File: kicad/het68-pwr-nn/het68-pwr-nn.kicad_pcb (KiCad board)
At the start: 2 copper layers, 140 x 80 mm, 64 parts, among them J1 CT_SEC, J2 USB_C, J3 VOUT, Q1 X0202MN, Q2 AO3400A, Q3 AO3401A, Q4 AO3400A

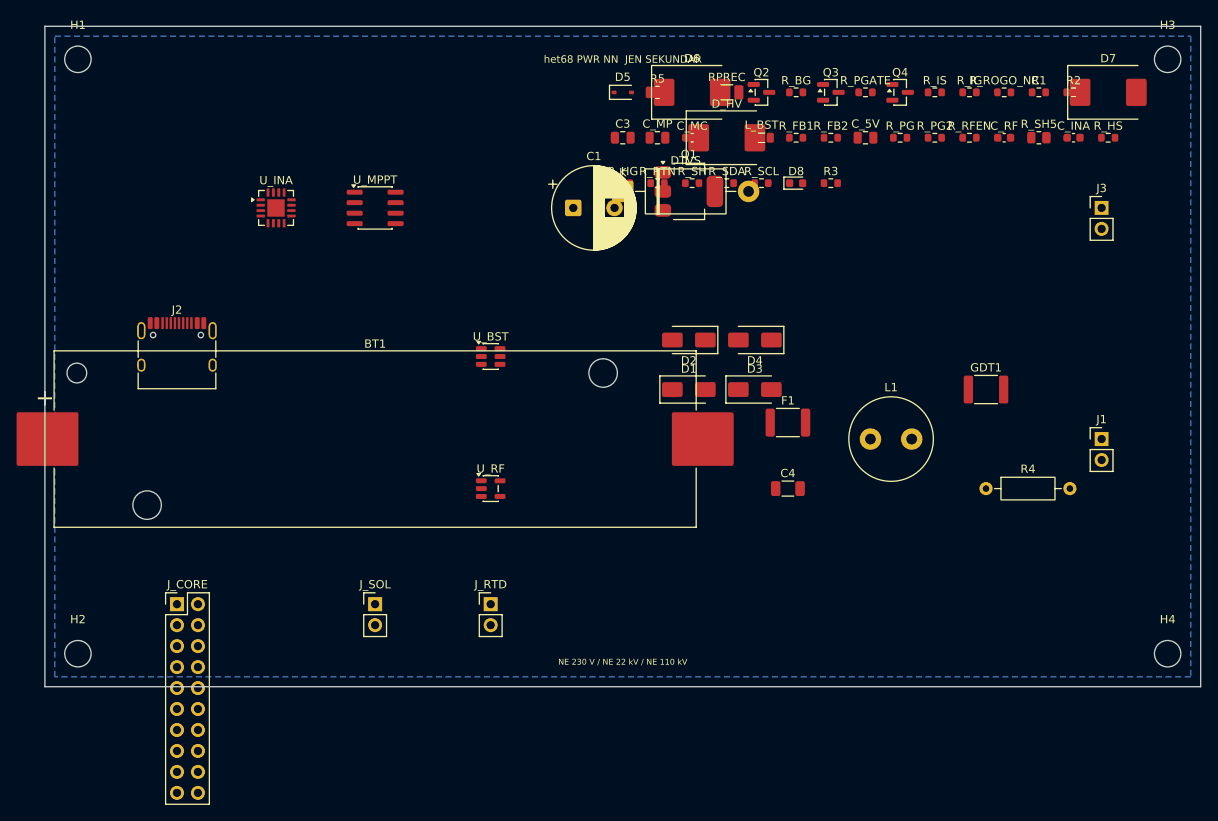
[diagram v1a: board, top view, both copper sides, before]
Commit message: Add a Core status LED and three buttons, and fit a 21700 holder.
RESET, BOOT and USER sit on the east edge with one SK6812; the power board uses a Keystone 1122 instead of an 18650 sled. Masks, schematics and JLCPCB gerber zips are in the tree.

Co-authored-by: Cursor <cursoragent@cursor.com>
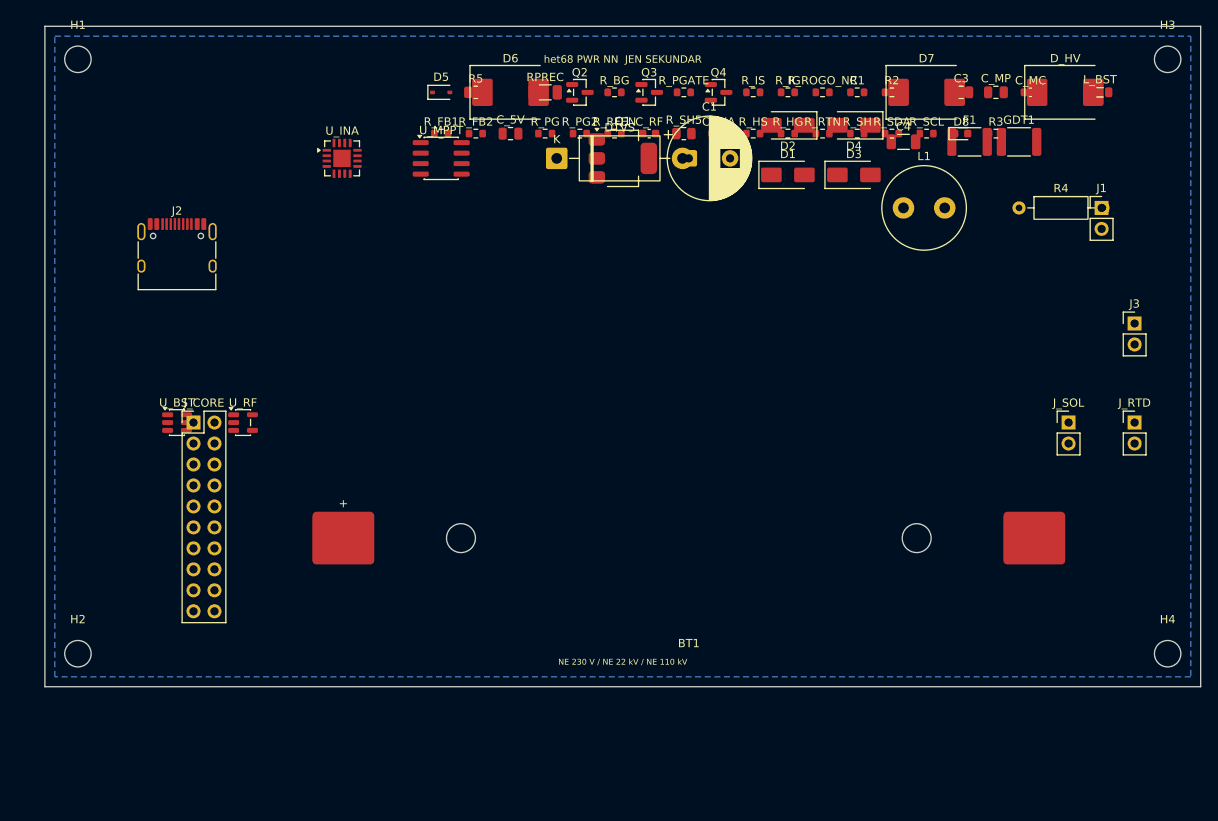
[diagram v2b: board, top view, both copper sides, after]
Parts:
- BT1: value LiFePO4_1S -> 21700; footprint Battery:BatteryHolder_Keystone_1042_1x18650 -> het68:Keystone_1122_21700
- moved J_SOL 86.8 mm to (124.0, 48.0)
- moved J_RTD 81.0 mm to (132.0, 48.0)
- moved C4 44.3 mm to (104.0, 14.0)
- moved R_HS 43.0 mm to (85.8, 13.0)
- moved C_5V 43.0 mm to (56.4, 13.0)
- moved C_INA 43.0 mm to (81.6, 13.0)
- moved C_RF 43.0 mm to (73.2, 13.0)
- moved R_FB1 43.0 mm to (48.0, 13.0)
- moved R_FB2 43.0 mm to (52.2, 13.0)
- moved R_PG2 43.0 mm to (64.8, 13.0)
- moved R_RFEN 43.0 mm to (69.0, 13.0)
- moved R_SH5 43.0 mm to (77.4, 13.0)
- moved R_PG 43.0 mm to (60.6, 13.0)
- moved C3 41.4 mm to (111.0, 8.00)
- moved C_MC 41.4 mm to (119.4, 8.00)
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
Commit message: Route signal copper on the five v4 boards and drop tracks that still short.
Core and the satellite have no copper shorts left. QFN-80 fanout and a few LVDS pairs stay open, and the power boards still have overlapping pads from placement.

Co-authored-by: Cursor <cursoragent@cursor.com>
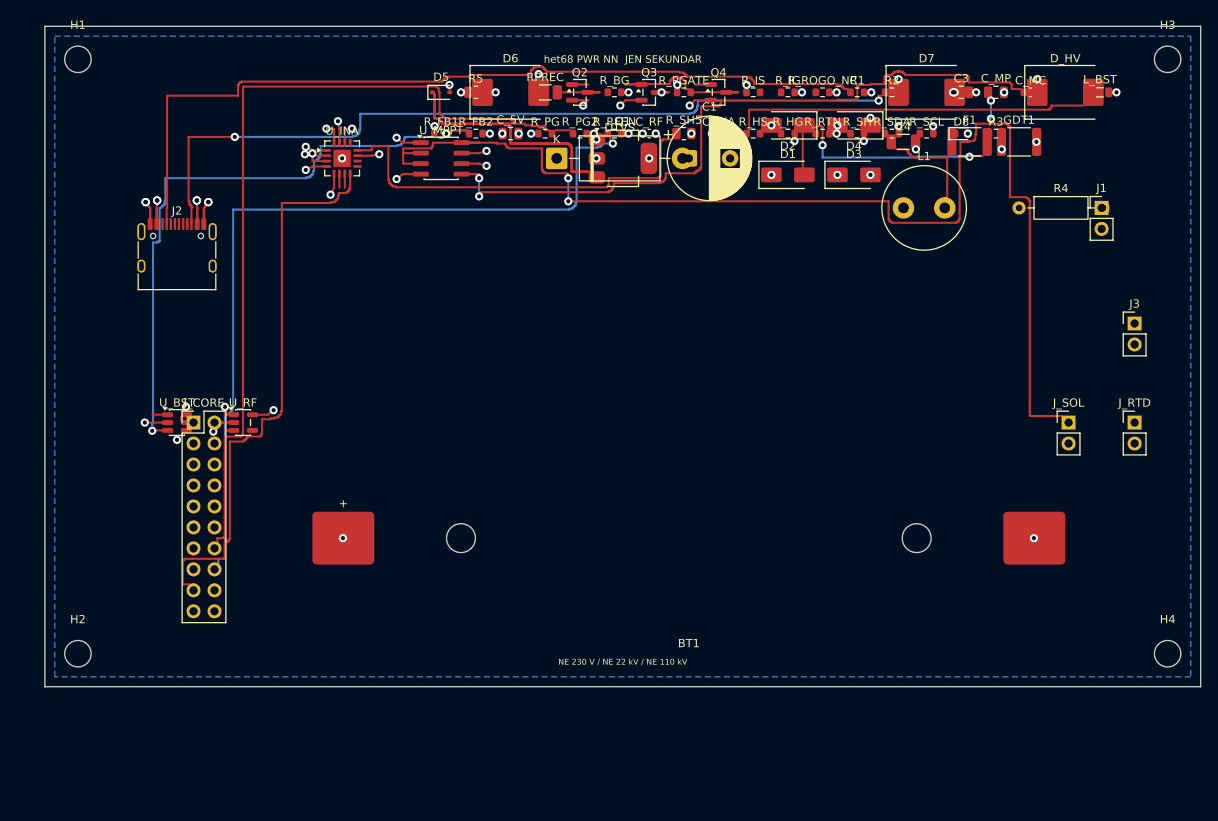
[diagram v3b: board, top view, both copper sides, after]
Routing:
- net SOL_P: track 0.00 -> 150.3 mm, vias 0 -> 4
- net CC1: track 0.00 -> 104.6 mm
- net PG_5V: track 0.00 -> 103.8 mm
- net EN_RF: track 0.00 -> 102.6 mm, vias 0 -> 1
- net CC2: track 0.00 -> 100.6 mm, vias 0 -> 2
- net MPPT_C: track 0.00 -> 88.2 mm, vias 0 -> 2
- net BST_FB: track 0.00 -> 78.4 mm, vias 0 -> 2
- net I2C0_ALERT: track 0.00 -> 72.3 mm
- net SCR_G: track 0.00 -> 58.2 mm
- net 5V_IN: track 0.00 -> 50.0 mm
- net VHARV: track 0.00 -> 49.3 mm, vias 0 -> 4
- net GND: track 0.00 -> 44.6 mm, vias 0 -> 34
- net AC1F: track 0.00 -> 32.0 mm, vias 0 -> 2
- net CHG_G: track 0.00 -> 19.1 mm
- net AC1L: track 0.00 -> 15.7 mm
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
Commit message: Fan out the RP2350B and finish the signal bridges that can leave the package.
Each QFN pin gets a 0.15 mm escape along its axis. The crystal moves off the north row so that corridor exists. Core and the satellite have no new shorts; a few center-row pins and some LVDS nets are still open.

Co-authored-by: Cursor <cursoragent@cursor.com>
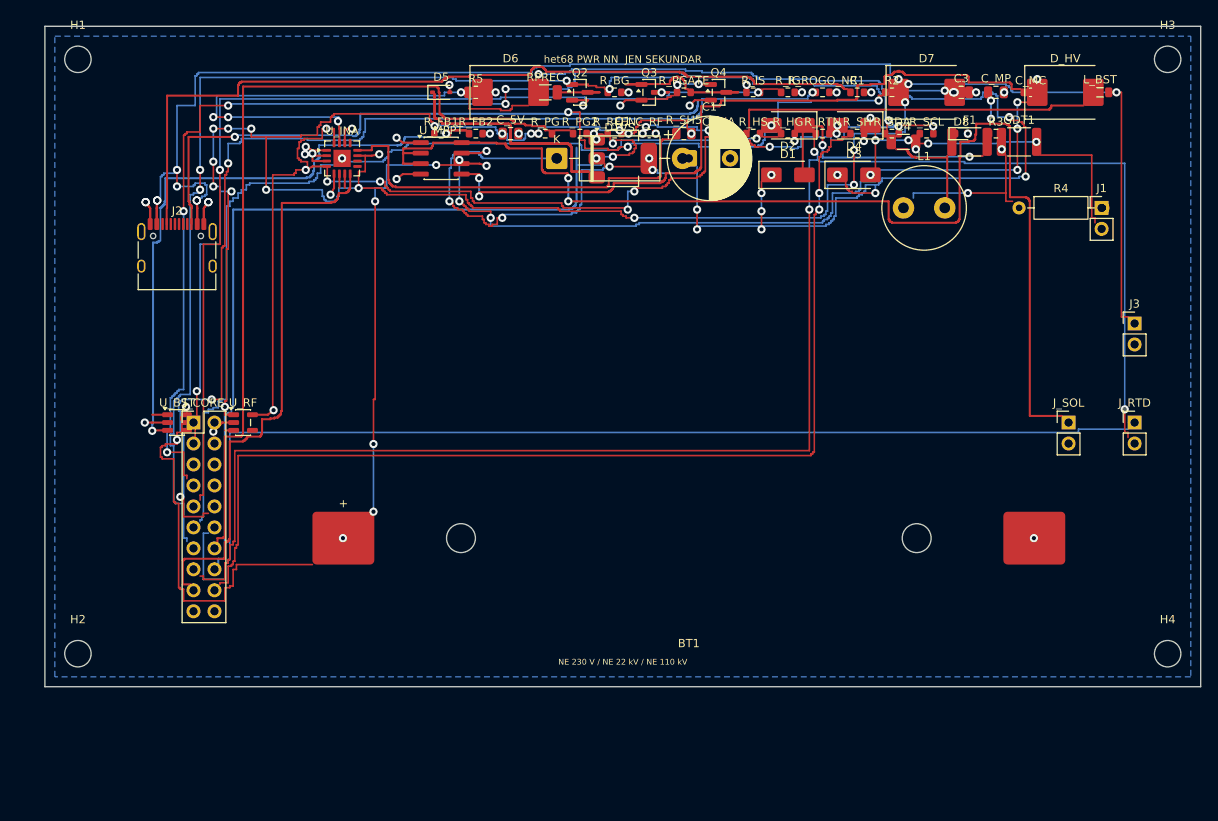
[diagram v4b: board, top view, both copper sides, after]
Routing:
- net +5V_ALWAYS: track 8.25 -> 306.7 mm, vias 9 -> 25
- net DC: track 8.18 -> 269.6 mm, vias 10 -> 24
- net PT1000_RTN: track 1.39 -> 201.8 mm, vias 0 -> 3
- net BAT: track 6.53 -> 198.3 mm, vias 6 -> 16
- net I2C0_SDA: track 3.10 -> 149.3 mm, vias 0 -> 6
- net +3V3_RF: track 9.83 -> 152.6 mm, vias 7 -> 14
- net ADC_PT1000: track 1.39 -> 137.8 mm
- net ADC_ROGO: track 1.39 -> 134.8 mm, vias 0 -> 4
- net SHIELD: track 1.39 -> 131.6 mm, vias 0 -> 2
- net VBUS: track 11.4 -> 136.0 mm, vias 6 -> 9
- net BURDEN_EN: track 5.27 -> 127.7 mm, vias 0 -> 5
- net ADC_I: track 1.39 -> 120.6 mm, vias 0 -> 2
- net ADC_HARVEST: track 1.39 -> 119.0 mm, vias 0 -> 1
- net AC2: track 4.62 -> 42.4 mm, vias 5 -> 8
- net CC2: track 100.6 -> 127.9 mm, vias 2 -> 4
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
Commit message: Put the satellite electronics on the back and clear the power-board pad shorts.
The outward face keeps only the microphone hole and the eight SK6812s. The DO-201 and the two regulators move off the header so the power boards no longer short pad to pad. Some LVDS, QSPI and GPIO nets are still open.

Co-authored-by: Cursor <cursoragent@cursor.com>
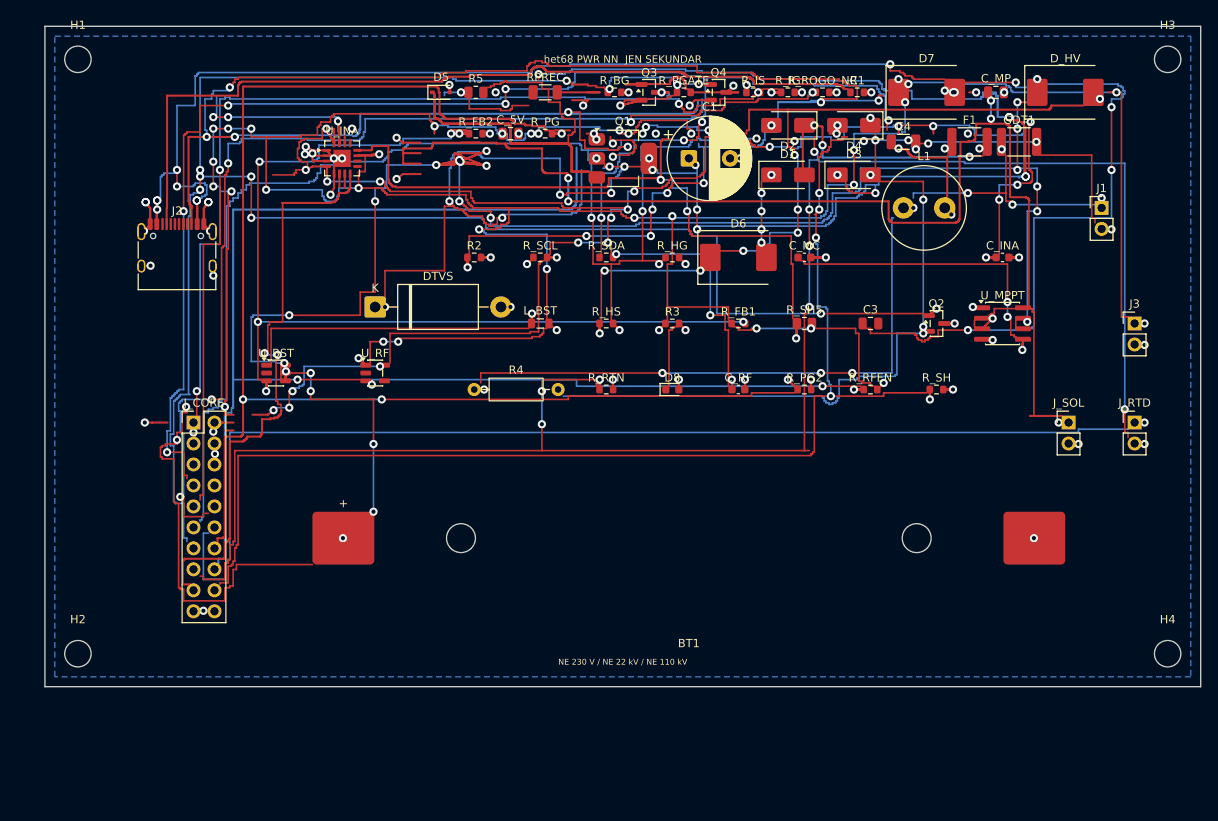
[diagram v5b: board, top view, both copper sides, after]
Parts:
- moved L_BST 73.4 mm to (60.0, 36.0)
- moved U_MPPT 70.9 mm to (116.0, 36.0)
- moved R4 69.6 mm to (52.0, 44.0)
- moved R2 54.4 mm to (52.0, 28.0)
- moved Q2 51.5 mm to (108.0, 36.0)
- moved R_SCL 49.1 mm to (60.0, 28.0)
- moved D8 46.8 mm to (76.0, 44.0)
- moved R3 45.4 mm to (76.0, 36.0)
- moved R_RFEN 43.8 mm to (100.0, 44.0)
- moved R_FB1 42.7 mm to (84.0, 36.0)
- moved R_PG2 41.2 mm to (92.0, 44.0)
- moved R_RTN 40.6 mm to (68.0, 44.0)
- moved R_SDA 37.7 mm to (68.0, 28.0)
- moved C_INA 37.5 mm to (116.0, 28.0)
- moved D6 34.1 mm to (84.0, 28.0)
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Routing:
- net +3V3_RF: track 152.6 -> 303.0 mm, vias 14 -> 28
- net CC2: track 127.9 -> 271.4 mm, vias 4 -> 13
- net VBUS: track 136.0 -> 276.3 mm, vias 9 -> 15
- net +5V_ALWAYS: track 306.7 -> 435.7 mm, vias 25 -> 38
- net BURDEN_EN: track 127.7 -> 250.5 mm, vias 5 -> 10
- net GND: track 44.6 -> 164.3 mm, vias 34 -> 56
- net BAT: track 198.3 -> 315.3 mm, vias 16 -> 26
- net PG_5V: track 103.8 -> 191.1 mm, vias 0 -> 4
- net AC1: track 19.1 -> 103.1 mm, vias 2 -> 9
- net EN_RF: track 111.1 -> 190.0 mm, vias 2 -> 6
- net AC2: track 42.4 -> 120.0 mm, vias 8 -> 12
- net DC: track 269.6 -> 329.2 mm, vias 24 -> 32
- net VHARV: track 49.3 -> 105.2 mm, vias 4 -> 12
- net BST_FB: track 78.7 -> 134.0 mm, vias 2 -> 6
- net 5V_IN: track 50.0 -> 95.2 mm, vias 0 -> 3
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
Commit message: Ship the furthest routed v4 boards with matching previews.
The satellite signal nets are closed, the five boards have no shorts, and the gerbers and renders follow this copper.

Co-authored-by: Cursor <cursoragent@cursor.com>
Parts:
- moved J_SOL 2.95 mm to (127.0, 48.0)
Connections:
- J2 pad A6: unconnected-(J2-D+-PadA6) -> (no net)
- J2 pad A7: unconnected-(J2-D--PadA7) -> (no net)
- J2 pad A8: unconnected-(J2-SBU1-PadA8) -> (no net)
- J2 pad B6: unconnected-(J2-D+-PadB6) -> (no net)
- J2 pad B7: unconnected-(J2-D--PadB7) -> (no net)
- J2 pad B8: unconnected-(J2-SBU2-PadB8) -> (no net)
- U_INA pad 10: unconnected-(U_INA-PV-Pad10) -> (no net)
- U_INA pad 13: unconnected-(U_INA-TC-Pad13) -> (no net)
- U_INA pad 9: unconnected-(U_INA-CRITICAL-Pad9) -> (no net)
- U_RF pad 4: unconnected-(U_RF-NC-Pad4) -> (no net)
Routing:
- net GND: track 164.3 -> 579.1 mm, vias 56 -> 65
- net ADC_PT1000: track 139.0 -> 146.1 mm, vias 1 -> 2
- net SOL_P: track 168.3 -> 172.9 mm
- net AC1: track 103.1 -> 107.6 mm
- net PT1000_RTN: track 228.0 -> 230.7 mm
- net AC2: track 120.0 -> 122.6 mm
- net ADC_ROGO: track 147.6 -> 149.2 mm
- net ADC_I: track 133.0 -> 134.6 mm
- net BURDEN_EN: track 250.5 -> 252.0 mm, vias 10 -> 11
- net I2C0_SDA: track 183.5 -> 185.0 mm
- net ADC_HARVEST: track 162.2 -> 163.4 mm, vias 5 -> 6
- net SHIELD: track 155.8 -> 156.9 mm
